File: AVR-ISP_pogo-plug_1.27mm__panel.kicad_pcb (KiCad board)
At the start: 2 copper layers, 96 x 82 mm, 112 parts, among them P1 CONN_6, P2 CONN_6

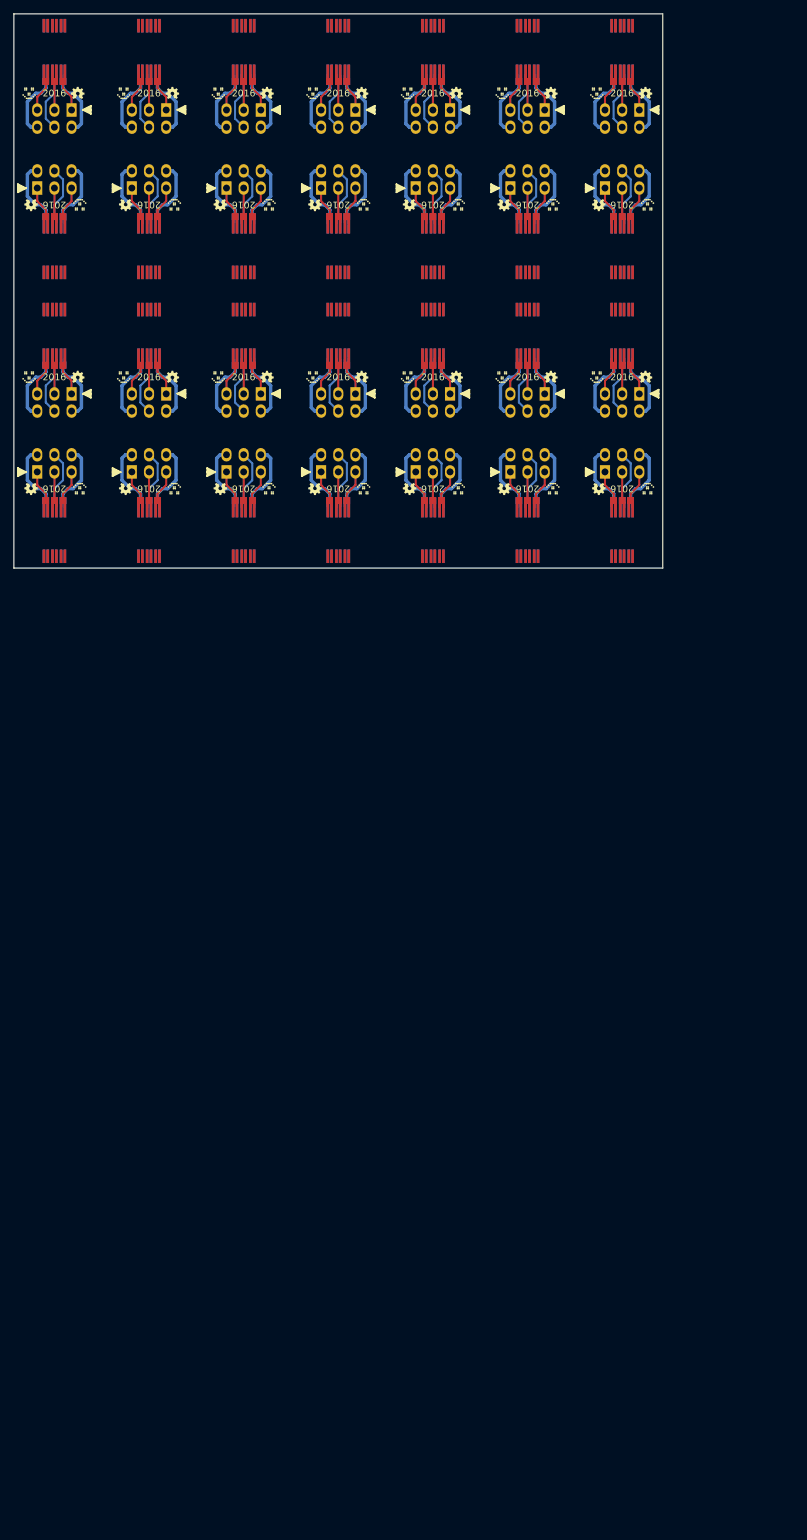
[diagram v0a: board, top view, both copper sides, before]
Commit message: Panel with mouse-bites instead of v-scoring.
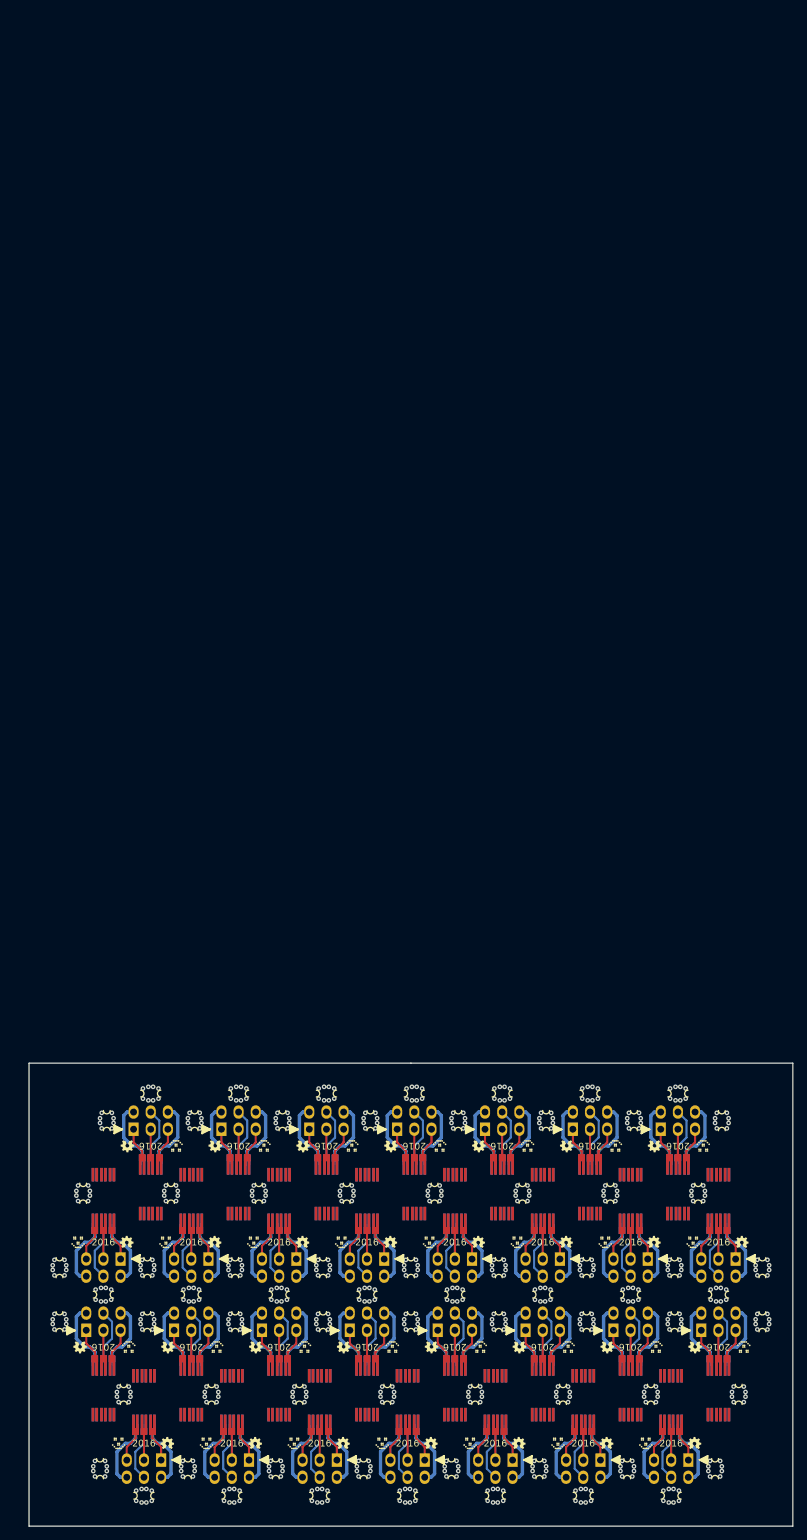
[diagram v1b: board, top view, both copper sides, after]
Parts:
- removed the G1 at (61.2, -97.8)
- removed the G1 at (67.8, -72.2)
- removed the G1 at (81.8, -72.2)
- removed the G1 at (89.2, -97.8)
- removed the G1 at (109.8, -72.2)
- removed the G1 at (117.2, -55.8)
- removed the G1 at (103.2, -55.8)
- removed the G1 at (95.8, -72.2)
- removed the G1 at (109.8, -114.2)
- removed the G1 at (95.8, -114.2)
- removed the G1 at (117.2, -97.8)
- removed the G1 at (61.2, -55.8)
- removed the G1 at (103.2, -97.8)
- removed the G1 at (47.2, -55.8)
- removed the G1 at (39.8, -72.2)
- removed the G1 at (47.2, -97.8)
- removed the G1 at (39.8, -114.2)
- removed the G1 at (25.8, -72.2)
- removed the G1 at (33.2, -55.8)
- removed the G1 at (33.2, -97.8)
- removed the G1 at (25.8, -114.2)
- removed the G1 at (53.8, -114.2)
- removed the G1 at (53.8, -72.2)
- removed the G1 at (89.2, -55.8)
- removed the G1 at (75.2, -55.8)
- removed the G1 at (67.8, -114.2)
- removed the G1 at (75.2, -97.8)
- removed the G1 at (81.8, -114.2)
- removed the G2 at (54.0, -97.7)
- removed the G2 at (75.0, -72.3)
- removed the G2 at (89.0, -72.3)
- removed the G2 at (82.0, -97.7)
- removed the G2 at (117.0, -72.3)
- removed the G2 at (103.0, -72.3)
- removed the G2 at (96.0, -55.7)
- removed the G2 at (110.0, -55.7)
- removed the G2 at (117.0, -114.3)
- removed the G2 at (103.0, -114.3)
- removed the G2 at (110.0, -97.7)
- removed the G2 at (54.0, -55.7)
- removed the G2 at (96.0, -97.7)
- removed the G2 at (40.0, -55.7)
- removed the G2 at (47.0, -72.3)
- removed the G2 at (40.0, -97.7)
- removed the G2 at (47.0, -114.3)
- removed the G2 at (33.0, -72.3)
- removed the G2 at (26.0, -55.7)
- removed the G2 at (33.0, -114.3)
- removed the G2 at (26.0, -97.7)
- removed the G2 at (61.0, -114.3)
- removed the G2 at (61.0, -72.3)
- removed the G2 at (82.0, -55.7)
- removed the G2 at (68.0, -55.7)
- removed the G2 at (68.0, -97.7)
- removed the G2 at (89.0, -114.3)
- removed the G2 at (75.0, -114.3)
- removed the P1 at (57.5, -101.5)
- removed the P1 at (85.5, -68.5)
- removed the P1 at (71.5, -68.5)
- removed the P1 at (85.5, -101.5)
- removed the P1 at (113.5, -68.5)
- removed the P1 at (99.5, -68.5)
- removed the P1 at (113.5, -59.5)
- removed the P1 at (99.5, -59.5)
- removed the P1 at (113.5, -110.5)
- removed the P1 at (99.5, -110.5)
- removed the P1 at (113.5, -101.5)
- removed the P1 at (57.5, -59.5)
- removed the P1 at (99.5, -101.5)
- removed the P1 at (43.5, -59.5)
- removed the P1 at (43.5, -68.5)
- removed the P1 at (43.5, -101.5)
- removed the P1 at (43.5, -110.5)
- removed the P1 at (29.5, -68.5)
- removed the P1 at (29.5, -59.5)
- removed the P1 at (29.5, -110.5)
- removed the P1 at (29.5, -101.5)
- removed the P1 at (57.5, -110.5)
- removed the P1 at (57.5, -68.5)
- removed the P1 at (85.5, -59.5)
- removed the P1 at (71.5, -59.5)
- removed the P1 at (71.5, -101.5)
- removed the P1 at (71.5, -110.5)
- removed the P1 at (85.5, -110.5)
- removed the P2 at (57.5, -91.5)
- removed the P2 at (85.5, -78.5)
- removed the P2 at (85.5, -91.5)
- removed the P2 at (71.5, -91.5)
- removed the P2 at (113.5, -78.5)
- removed the P2 at (113.5, -49.5)
- removed the P2 at (99.5, -49.5)
- removed the P2 at (99.5, -78.5)
- removed the P2 at (113.5, -120.5)
- removed the P2 at (99.5, -120.5)
- removed the P2 at (113.5, -91.5)
- removed the P2 at (57.5, -49.5)
- removed the P2 at (99.5, -91.5)
- removed the P2 at (43.5, -49.5)
- removed the P2 at (43.5, -91.5)
- removed the P2 at (43.5, -78.5)
- removed the P2 at (43.5, -120.5)
- removed the P2 at (29.5, -78.5)
- removed the P2 at (29.5, -49.5)
- removed the P2 at (29.5, -120.5)
- removed the P2 at (29.5, -91.5)
- removed the P2 at (57.5, -120.5)
- removed the P2 at (57.5, -78.5)
- removed the P2 at (85.5, -49.5)
- removed the P2 at (71.5, -49.5)
- removed the P2 at (85.5, -120.5)
- removed the P2 at (71.5, -120.5)
- removed the P2 at (71.5, -78.5)
- added G1: LED_smile_silkscreen_2mm, LED_smile_silkscreen_2mm, F.Cu at (40.5, 71.2)
- added G1: LED_smile_silkscreen_2mm, LED_smile_silkscreen_2mm, F.Cu at (66.5, 71.2)
- added G1: LED_smile_silkscreen_2mm, LED_smile_silkscreen_2mm, F.Cu at (53.5, 71.3)
- added G1: LED_smile_silkscreen_2mm, LED_smile_silkscreen_2mm, F.Cu at (52.0, 85.5)
- added G1: LED_smile_silkscreen_2mm, LED_smile_silkscreen_2mm, F.Cu at (117.0, 85.5)
- added G1: LED_smile_silkscreen_2mm, LED_smile_silkscreen_2mm, F.Cu at (131.5, 71.2)
- added G1: LED_smile_silkscreen_2mm, LED_smile_silkscreen_2mm, F.Cu at (91.0, 85.5)
- added G1: LED_smile_silkscreen_2mm, LED_smile_silkscreen_2mm, F.Cu at (118.5, 71.3)
- added G1: LED_smile_silkscreen_2mm, LED_smile_silkscreen_2mm, F.Cu at (73.5, 41.5)
- added G1: LED_smile_silkscreen_2mm, LED_smile_silkscreen_2mm, F.Cu at (60.5, 41.5)
- added G1: LED_smile_silkscreen_2mm, LED_smile_silkscreen_2mm, F.Cu at (125.5, 41.5)
- added G1: LED_smile_silkscreen_2mm, LED_smile_silkscreen_2mm, F.Cu at (124.0, 55.8)
- added G1: LED_smile_silkscreen_2mm, LED_smile_silkscreen_2mm, F.Cu at (86.5, 41.5)
- added G1: LED_smile_silkscreen_2mm, LED_smile_silkscreen_2mm, F.Cu at (47.5, 41.5)
- added G1: LED_smile_silkscreen_2mm, LED_smile_silkscreen_2mm, F.Cu at (99.5, 41.5)
- added G1: LED_smile_silkscreen_2mm, LED_smile_silkscreen_2mm, F.Cu at (112.5, 41.5)
- added G1: LED_smile_silkscreen_2mm, LED_smile_silkscreen_2mm, F.Cu at (111.0, 55.8)
- added G1: LED_smile_silkscreen_2mm, LED_smile_silkscreen_2mm, F.Cu at (98.0, 55.8)
- added G1: LED_smile_silkscreen_2mm, LED_smile_silkscreen_2mm, F.Cu at (85.0, 55.8)
- added G1: LED_smile_silkscreen_2mm, LED_smile_silkscreen_2mm, F.Cu at (59.0, 55.8)
- added G1: LED_smile_silkscreen_2mm, LED_smile_silkscreen_2mm, F.Cu at (72.0, 55.8)
- added G1: LED_smile_silkscreen_2mm, LED_smile_silkscreen_2mm, F.Cu at (46.0, 55.8)
- added G1: LED_smile_silkscreen_2mm, LED_smile_silkscreen_2mm, F.Cu at (79.5, 71.2)
- added G1: LED_smile_silkscreen_2mm, LED_smile_silkscreen_2mm, F.Cu at (33.0, 55.8)
- added G1: LED_smile_silkscreen_2mm, LED_smile_silkscreen_2mm, F.Cu at (78.0, 85.5)
- added G1: LED_smile_silkscreen_2mm, LED_smile_silkscreen_2mm, F.Cu at (105.5, 71.3)
- added G1: LED_smile_silkscreen_2mm, LED_smile_silkscreen_2mm, F.Cu at (104.0, 85.5)
- added G1: LED_smile_silkscreen_2mm, LED_smile_silkscreen_2mm, F.Cu at (92.5, 71.2)
- added G1: LED_smile_silkscreen_2mm, LED_smile_silkscreen_2mm, F.Cu at (39.0, 85.5)
- added G1: LED_smile_silkscreen_2mm, LED_smile_silkscreen_2mm, F.Cu at (65.0, 85.5)
- added G2: OSHW-logo_silkscreen_2mm, OSHW-logo_silkscreen_2mm, F.Cu at (33.3, 71.3)
- added G2: OSHW-logo_silkscreen_2mm, OSHW-logo_silkscreen_2mm, F.Cu at (59.3, 71.3)
- added G2: OSHW-logo_silkscreen_2mm, OSHW-logo_silkscreen_2mm, F.Cu at (46.3, 71.3)
- added G2: OSHW-logo_silkscreen_2mm, OSHW-logo_silkscreen_2mm, F.Cu at (59.2, 85.5)
- added G2: OSHW-logo_silkscreen_2mm, OSHW-logo_silkscreen_2mm, F.Cu at (111.2, 85.5)
- added G2: OSHW-logo_silkscreen_2mm, OSHW-logo_silkscreen_2mm, F.Cu at (124.2, 85.5)
- added G2: OSHW-logo_silkscreen_2mm, OSHW-logo_silkscreen_2mm, F.Cu at (124.3, 71.3)
- added G2: OSHW-logo_silkscreen_2mm, OSHW-logo_silkscreen_2mm, F.Cu at (111.3, 71.3)
- added G2: OSHW-logo_silkscreen_2mm, OSHW-logo_silkscreen_2mm, F.Cu at (66.3, 41.6)
- added G2: OSHW-logo_silkscreen_2mm, OSHW-logo_silkscreen_2mm, F.Cu at (53.3, 41.5)
- added G2: OSHW-logo_silkscreen_2mm, OSHW-logo_silkscreen_2mm, F.Cu at (118.3, 41.6)
- added G2: OSHW-logo_silkscreen_2mm, OSHW-logo_silkscreen_2mm, F.Cu at (131.2, 55.7)
- added G2: OSHW-logo_silkscreen_2mm, OSHW-logo_silkscreen_2mm, F.Cu at (79.3, 41.5)
- added G2: OSHW-logo_silkscreen_2mm, OSHW-logo_silkscreen_2mm, F.Cu at (40.3, 41.5)
- added G2: OSHW-logo_silkscreen_2mm, OSHW-logo_silkscreen_2mm, F.Cu at (92.3, 41.6)
- added G2: OSHW-logo_silkscreen_2mm, OSHW-logo_silkscreen_2mm, F.Cu at (105.3, 41.5)
- added G2: OSHW-logo_silkscreen_2mm, OSHW-logo_silkscreen_2mm, F.Cu at (118.2, 55.7)
- added G2: OSHW-logo_silkscreen_2mm, OSHW-logo_silkscreen_2mm, F.Cu at (92.2, 55.7)
- added G2: OSHW-logo_silkscreen_2mm, OSHW-logo_silkscreen_2mm, F.Cu at (105.2, 55.7)
- added G2: OSHW-logo_silkscreen_2mm, OSHW-logo_silkscreen_2mm, F.Cu at (66.2, 55.7)
- added G2: OSHW-logo_silkscreen_2mm, OSHW-logo_silkscreen_2mm, F.Cu at (79.2, 55.7)
- added G2: OSHW-logo_silkscreen_2mm, OSHW-logo_silkscreen_2mm, F.Cu at (53.2, 55.7)
- added G2: OSHW-logo_silkscreen_2mm, OSHW-logo_silkscreen_2mm, F.Cu at (72.3, 71.3)
- added G2: OSHW-logo_silkscreen_2mm, OSHW-logo_silkscreen_2mm, F.Cu at (40.2, 55.7)
- added G2: OSHW-logo_silkscreen_2mm, OSHW-logo_silkscreen_2mm, F.Cu at (85.3, 71.3)
- added G2: OSHW-logo_silkscreen_2mm, OSHW-logo_silkscreen_2mm, F.Cu at (85.2, 85.5)
- added G2: OSHW-logo_silkscreen_2mm, OSHW-logo_silkscreen_2mm, F.Cu at (98.3, 71.3)
- added G2: OSHW-logo_silkscreen_2mm, OSHW-logo_silkscreen_2mm, F.Cu at (98.2, 85.5)
- added G2: OSHW-logo_silkscreen_2mm, OSHW-logo_silkscreen_2mm, F.Cu at (72.2, 85.5)
- added G2: OSHW-logo_silkscreen_2mm, OSHW-logo_silkscreen_2mm, F.Cu at (46.2, 85.5)
- added P1: CONN_6, my_parts:MADW__PIN_ARRAY_3x2_2.54mm, F.Cu at (36.8, 67.5)
- added P1: CONN_6, my_parts:MADW__PIN_ARRAY_3x2_2.54mm, F.Cu at (49.7, 67.5)
- added P1: CONN_6, my_parts:MADW__PIN_ARRAY_3x2_2.54mm, F.Cu at (107.8, 89.2)
- added P1: CONN_6, my_parts:MADW__PIN_ARRAY_3x2_2.54mm, F.Cu at (120.8, 89.2)
- added P1: CONN_6, my_parts:MADW__PIN_ARRAY_3x2_2.54mm, F.Cu at (127.8, 67.5)
- added P1: CONN_6, my_parts:MADW__PIN_ARRAY_3x2_2.54mm, F.Cu at (94.8, 89.2)
- added P1: CONN_6, my_parts:MADW__PIN_ARRAY_3x2_2.54mm, F.Cu at (81.8, 89.2)
- added P1: CONN_6, my_parts:MADW__PIN_ARRAY_3x2_2.54mm, F.Cu at (114.8, 67.5)
- added P1: CONN_6, my_parts:MADW__PIN_ARRAY_3x2_2.54mm, F.Cu at (69.7, 37.8)
- added P1: CONN_6, my_parts:MADW__PIN_ARRAY_3x2_2.54mm, F.Cu at (56.8, 37.8)
- added P1: CONN_6, my_parts:MADW__PIN_ARRAY_3x2_2.54mm, F.Cu at (121.8, 37.8)
- added P1: CONN_6, my_parts:MADW__PIN_ARRAY_3x2_2.54mm, F.Cu at (127.8, 59.5)
- added P1: CONN_6, my_parts:MADW__PIN_ARRAY_3x2_2.54mm, F.Cu at (82.7, 37.8)
- added P1: CONN_6, my_parts:MADW__PIN_ARRAY_3x2_2.54mm, F.Cu at (43.7, 37.7)
- added P1: CONN_6, my_parts:MADW__PIN_ARRAY_3x2_2.54mm, F.Cu at (95.8, 37.7)
- added P1: CONN_6, my_parts:MADW__PIN_ARRAY_3x2_2.54mm, F.Cu at (108.8, 37.8)
- added P1: CONN_6, my_parts:MADW__PIN_ARRAY_3x2_2.54mm, F.Cu at (114.8, 59.5)
- added P1: CONN_6, my_parts:MADW__PIN_ARRAY_3x2_2.54mm, F.Cu at (88.8, 59.5)
- added P1: CONN_6, my_parts:MADW__PIN_ARRAY_3x2_2.54mm, F.Cu at (101.8, 59.5)
- added P1: CONN_6, my_parts:MADW__PIN_ARRAY_3x2_2.54mm, F.Cu at (62.8, 59.5)
- added P1: CONN_6, my_parts:MADW__PIN_ARRAY_3x2_2.54mm, F.Cu at (75.8, 59.5)
- added P1: CONN_6, my_parts:MADW__PIN_ARRAY_3x2_2.54mm, F.Cu at (49.8, 59.5)
- added P1: CONN_6, my_parts:MADW__PIN_ARRAY_3x2_2.54mm, F.Cu at (75.7, 67.5)
- added P1: CONN_6, my_parts:MADW__PIN_ARRAY_3x2_2.54mm, F.Cu at (36.8, 59.5)
- added P1: CONN_6, my_parts:MADW__PIN_ARRAY_3x2_2.54mm, F.Cu at (101.8, 67.5)
- added P1: CONN_6, my_parts:MADW__PIN_ARRAY_3x2_2.54mm, F.Cu at (88.7, 67.5)
- added P1: CONN_6, my_parts:MADW__PIN_ARRAY_3x2_2.54mm, F.Cu at (68.8, 89.2)
- added P1: CONN_6, my_parts:MADW__PIN_ARRAY_3x2_2.54mm, F.Cu at (55.8, 89.2)
- added P1: CONN_6, my_parts:MADW__PIN_ARRAY_3x2_2.54mm, F.Cu at (42.8, 89.2)
- added P1: CONN_6, my_parts:MADW__PIN_ARRAY_3x2_2.54mm, F.Cu at (62.8, 67.5)
- added P2: CONN_6, MADW__PIN_ARRAY_3x2_1.27mm, F.Cu at (36.8, 77.5)
- added P2: CONN_6, MADW__PIN_ARRAY_3x2_1.27mm, F.Cu at (68.8, 79.2)
- added P2: CONN_6, MADW__PIN_ARRAY_3x2_1.27mm, F.Cu at (49.8, 77.5)
- added P2: CONN_6, MADW__PIN_ARRAY_3x2_1.27mm, F.Cu at (55.8, 79.2)
- added P2: CONN_6, MADW__PIN_ARRAY_3x2_1.27mm, F.Cu at (42.8, 79.2)
- added P2: CONN_6, MADW__PIN_ARRAY_3x2_1.27mm, F.Cu at (120.8, 79.2)
- added P2: CONN_6, MADW__PIN_ARRAY_3x2_1.27mm, F.Cu at (114.7, 77.5)
- added P2: CONN_6, MADW__PIN_ARRAY_3x2_1.27mm, F.Cu at (127.8, 77.5)
- added P2: CONN_6, MADW__PIN_ARRAY_3x2_1.27mm, F.Cu at (69.8, 47.8)
- added P2: CONN_6, MADW__PIN_ARRAY_3x2_1.27mm, F.Cu at (82.8, 47.8)
- added P2: CONN_6, MADW__PIN_ARRAY_3x2_1.27mm, F.Cu at (121.8, 47.8)
- added P2: CONN_6, MADW__PIN_ARRAY_3x2_1.27mm, F.Cu at (127.8, 49.5)
- added P2: CONN_6, MADW__PIN_ARRAY_3x2_1.27mm, F.Cu at (56.8, 47.8)
- added P2: CONN_6, MADW__PIN_ARRAY_3x2_1.27mm, F.Cu at (43.8, 47.7)
- added P2: CONN_6, MADW__PIN_ARRAY_3x2_1.27mm, F.Cu at (95.8, 47.8)
- added P2: CONN_6, MADW__PIN_ARRAY_3x2_1.27mm, F.Cu at (108.7, 47.7)
- added P2: CONN_6, MADW__PIN_ARRAY_3x2_1.27mm, F.Cu at (114.8, 49.5)
- added P2: CONN_6, MADW__PIN_ARRAY_3x2_1.27mm, F.Cu at (101.8, 49.5)
- added P2: CONN_6, MADW__PIN_ARRAY_3x2_1.27mm, F.Cu at (88.8, 49.5)
- added P2: CONN_6, MADW__PIN_ARRAY_3x2_1.27mm, F.Cu at (62.8, 49.5)
- added P2: CONN_6, MADW__PIN_ARRAY_3x2_1.27mm, F.Cu at (75.8, 49.5)
- added P2: CONN_6, MADW__PIN_ARRAY_3x2_1.27mm, F.Cu at (49.8, 49.5)
- added P2: CONN_6, MADW__PIN_ARRAY_3x2_1.27mm, F.Cu at (81.8, 79.2)
- added P2: CONN_6, MADW__PIN_ARRAY_3x2_1.27mm, F.Cu at (36.8, 49.5)
- added P2: CONN_6, MADW__PIN_ARRAY_3x2_1.27mm, F.Cu at (75.8, 77.5)
- added P2: CONN_6, MADW__PIN_ARRAY_3x2_1.27mm, F.Cu at (107.8, 79.2)
- added P2: CONN_6, MADW__PIN_ARRAY_3x2_1.27mm, F.Cu at (101.8, 77.5)
- added P2: CONN_6, MADW__PIN_ARRAY_3x2_1.27mm, F.Cu at (94.8, 79.2)
- added P2: CONN_6, MADW__PIN_ARRAY_3x2_1.27mm, F.Cu at (88.8, 77.5)
- added P2: CONN_6, MADW__PIN_ARRAY_3x2_1.27mm, F.Cu at (62.8, 77.5)
- added mouse-bite-1mm-slot: VAL**, Panelization:mouse-bite-1mm-slot, F.Cu at (33.8, 48.5)
- added mouse-bite-1mm-slot: VAL**, Panelization:mouse-bite-1mm-slot, F.Cu at (91.8, 78.2)
- added mouse-bite-1mm-slot: VAL**, Panelization:mouse-bite-1mm-slot, F.Cu at (95.2, 67.5)
- added mouse-bite-1mm-slot: VAL**, Panelization:mouse-bite-1mm-slot, F.Cu at (75.2, 89.2)
- added mouse-bite-1mm-slot: VAL**, Panelization:mouse-bite-1mm-slot, F.Cu at (62.2, 89.2)
- added mouse-bite-1mm-slot: VAL**, Panelization:mouse-bite-1mm-slot, F.Cu at (49.2, 89.2)
- added mouse-bite-1mm-slot: VAL**, Panelization:mouse-bite-1mm-slot, F.Cu at (69.2, 67.5)
- added mouse-bite-1mm-slot: VAL**, Panelization:mouse-bite-1mm-slot, F.Cu at (56.2, 67.5)
- added mouse-bite-1mm-slot: VAL**, Panelization:mouse-bite-1mm-slot, F.Cu at (65.8, 78.2)
- added mouse-bite-1mm-slot: VAL**, Panelization:mouse-bite-1mm-slot, F.Cu at (52.8, 78.2)
- added mouse-bite-1mm-slot: VAL**, Panelization:mouse-bite-1mm-slot, F.Cu at (101.2, 89.2)
- added mouse-bite-1mm-slot: VAL**, Panelization:mouse-bite-1mm-slot, F.Cu at (128.2, 37.8)
- added mouse-bite-1mm-slot: VAL**, Panelization:mouse-bite-1mm-slot, F.Cu at (114.2, 89.2)
- added mouse-bite-1mm-slot: VAL**, Panelization:mouse-bite-1mm-slot, F.Cu at (117.8, 78.2)
- added mouse-bite-1mm-slot: VAL**, Panelization:mouse-bite-1mm-slot, F.Cu at (88.2, 89.2)
- added mouse-bite-1mm-slot: VAL**, Panelization:mouse-bite-1mm-slot, F.Cu at (121.2, 67.5)
- added mouse-bite-1mm-slot: VAL**, Panelization:mouse-bite-1mm-slot, F.Cu at (111.8, 48.5)
- added mouse-bite-1mm-slot: VAL**, Panelization:mouse-bite-1mm-slot, F.Cu at (98.8, 48.5)
- added mouse-bite-1mm-slot: VAL**, Panelization:mouse-bite-1mm-slot, F.Cu at (85.8, 48.5)
- added mouse-bite-1mm-slot: VAL**, Panelization:mouse-bite-1mm-slot, F.Cu at (72.8, 48.5)
- added mouse-bite-1mm-slot: VAL**, Panelization:mouse-bite-1mm-slot, F.Cu at (59.8, 48.5)
- added mouse-bite-1mm-slot: VAL**, Panelization:mouse-bite-1mm-slot, F.Cu at (76.2, 37.8)
- added mouse-bite-1mm-slot: VAL**, Panelization:mouse-bite-1mm-slot, F.Cu at (124.8, 48.5)
- added mouse-bite-1mm-slot: VAL**, Panelization:mouse-bite-1mm-slot, F.Cu at (63.2, 37.7)
- added mouse-bite-1mm-slot: VAL**, Panelization:mouse-bite-1mm-slot, F.Cu at (89.2, 37.8)
- added mouse-bite-1mm-slot: VAL**, Panelization:mouse-bite-1mm-slot, F.Cu at (50.2, 37.8)
- added mouse-bite-1mm-slot: VAL**, Panelization:mouse-bite-1mm-slot, F.Cu at (102.2, 37.7)
- added mouse-bite-1mm-slot: VAL**, Panelization:mouse-bite-1mm-slot, F.Cu at (115.2, 37.8)
- added mouse-bite-1mm-slot: VAL**, Panelization:mouse-bite-1mm-slot, F.Cu at (82.2, 59.5)
- added mouse-bite-1mm-slot: VAL**, Panelization:mouse-bite-1mm-slot, F.Cu at (108.2, 59.5)
- added mouse-bite-1mm-slot: VAL**, Panelization:mouse-bite-1mm-slot, F.Cu at (95.2, 59.5)
- added mouse-bite-1mm-slot: VAL**, Panelization:mouse-bite-1mm-slot, F.Cu at (56.2, 59.5)
- added mouse-bite-1mm-slot: VAL**, Panelization:mouse-bite-1mm-slot, F.Cu at (69.2, 59.5)
- added mouse-bite-1mm-slot: VAL**, Panelization:mouse-bite-1mm-slot, F.Cu at (130.8, 78.2)
- added mouse-bite-1mm-slot: VAL**, Panelization:mouse-bite-1mm-slot, F.Cu at (43.2, 59.5)
- added mouse-bite-1mm-slot: VAL**, Panelization:mouse-bite-1mm-slot, F.Cu at (46.8, 48.5)
- added mouse-bite-1mm-slot: VAL**, Panelization:mouse-bite-1mm-slot, F.Cu at (49.8, 63.5)
- added mouse-bite-1mm-slot: VAL**, Panelization:mouse-bite-1mm-slot, F.Cu at (62.8, 63.5)
- added mouse-bite-1mm-slot: VAL**, Panelization:mouse-bite-1mm-slot, F.Cu at (75.8, 63.5)
- added mouse-bite-1mm-slot: VAL**, Panelization:mouse-bite-1mm-slot, F.Cu at (88.8, 63.5)
- added mouse-bite-1mm-slot: VAL**, Panelization:mouse-bite-1mm-slot, F.Cu at (101.8, 63.5)
- added mouse-bite-1mm-slot: VAL**, Panelization:mouse-bite-1mm-slot, F.Cu at (114.8, 63.5)
- added mouse-bite-1mm-slot: VAL**, Panelization:mouse-bite-1mm-slot, F.Cu at (36.8, 63.5)
- added mouse-bite-1mm-slot: VAL**, Panelization:mouse-bite-1mm-slot, F.Cu at (127.8, 63.5)
- added mouse-bite-1mm-slot: VAL**, Panelization:mouse-bite-1mm-slot, F.Cu at (39.8, 78.2)
- added mouse-bite-1mm-slot: VAL**, Panelization:mouse-bite-1mm-slot, F.Cu at (121.8, 33.8)
- added mouse-bite-1mm-slot: VAL**, Panelization:mouse-bite-1mm-slot, F.Cu at (108.8, 33.8)
- added mouse-bite-1mm-slot: VAL**, Panelization:mouse-bite-1mm-slot, F.Cu at (95.8, 33.8)
- added mouse-bite-1mm-slot: VAL**, Panelization:mouse-bite-1mm-slot, F.Cu at (82.8, 33.8)
- added mouse-bite-1mm-slot: VAL**, Panelization:mouse-bite-1mm-slot, F.Cu at (69.8, 33.8)
- added mouse-bite-1mm-slot: VAL**, Panelization:mouse-bite-1mm-slot, F.Cu at (56.8, 33.8)
- added mouse-bite-1mm-slot: VAL**, Panelization:mouse-bite-1mm-slot, F.Cu at (43.8, 33.8)
- added mouse-bite-1mm-slot: VAL**, Panelization:mouse-bite-1mm-slot, F.Cu at (42.8, 93.2)
- added mouse-bite-1mm-slot: VAL**, Panelization:mouse-bite-1mm-slot, F.Cu at (55.8, 93.2)
- added mouse-bite-1mm-slot: VAL**, Panelization:mouse-bite-1mm-slot, F.Cu at (68.8, 93.2)
- added mouse-bite-1mm-slot: VAL**, Panelization:mouse-bite-1mm-slot, F.Cu at (82.2, 67.5)
- added mouse-bite-1mm-slot: VAL**, Panelization:mouse-bite-1mm-slot, F.Cu at (81.8, 93.2)
- added mouse-bite-1mm-slot: VAL**, Panelization:mouse-bite-1mm-slot, F.Cu at (94.8, 93.2)
- added mouse-bite-1mm-slot: VAL**, Panelization:mouse-bite-1mm-slot, F.Cu at (107.8, 93.2)
- added mouse-bite-1mm-slot: VAL**, Panelization:mouse-bite-1mm-slot, F.Cu at (120.8, 93.2)
- added mouse-bite-1mm-slot: VAL**, Panelization:mouse-bite-1mm-slot, F.Cu at (30.2, 59.5)
- added mouse-bite-1mm-slot: VAL**, Panelization:mouse-bite-1mm-slot, F.Cu at (30.2, 67.5)
- added mouse-bite-1mm-slot: VAL**, Panelization:mouse-bite-1mm-slot, F.Cu at (134.2, 67.5)
- added mouse-bite-1mm-slot: VAL**, Panelization:mouse-bite-1mm-slot, F.Cu at (134.2, 59.5)
- added mouse-bite-1mm-slot: VAL**, Panelization:mouse-bite-1mm-slot, F.Cu at (36.2, 89.2)
- added mouse-bite-1mm-slot: VAL**, Panelization:mouse-bite-1mm-slot, F.Cu at (127.2, 89.2)
- added mouse-bite-1mm-slot: VAL**, Panelization:mouse-bite-1mm-slot, F.Cu at (78.8, 78.2)
- added mouse-bite-1mm-slot: VAL**, Panelization:mouse-bite-1mm-slot, F.Cu at (121.2, 59.5)
- added mouse-bite-1mm-slot: VAL**, Panelization:mouse-bite-1mm-slot, F.Cu at (43.2, 67.5)
- added mouse-bite-1mm-slot: VAL**, Panelization:mouse-bite-1mm-slot, F.Cu at (37.2, 37.8)
- added mouse-bite-1mm-slot: VAL**, Panelization:mouse-bite-1mm-slot, F.Cu at (108.2, 67.5)
- added mouse-bite-1mm-slot: VAL**, Panelization:mouse-bite-1mm-slot, F.Cu at (104.8, 78.2)
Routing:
- net /V-target: track 328.7 -> 352.2 mm
- net /GND: track 328.7 -> 352.2 mm
- net /MOSI: track 281.9 -> 302.1 mm
- net /RESET: track 196.0 -> 210.0 mm
- net /MISO: track 196.0 -> 210.0 mm
- net /SCK: track 180.8 -> 193.7 mm
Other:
- board size 96 x 82 mm -> 113 x 68.5 mm
- board text removed: "ROUTE"
- board text removed: "V-score"

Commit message: Well... routing paths should really be correct.
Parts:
- removed the G1 at (40.5, 71.2)
- removed the G1 at (66.5, 71.2)
- removed the G1 at (53.5, 71.3)
- removed the G1 at (52.0, 85.5)
- removed the G1 at (117.0, 85.5)
- removed the G1 at (131.5, 71.2)
- removed the G1 at (91.0, 85.5)
- removed the G1 at (118.5, 71.3)
- removed the G1 at (79.5, 71.2)
- removed the G1 at (78.0, 85.5)
- removed the G1 at (105.5, 71.3)
- removed the G1 at (104.0, 85.5)
- removed the G1 at (92.5, 71.2)
- removed the G1 at (39.0, 85.5)
- removed the G1 at (65.0, 85.5)
- removed the G2 at (59.3, 71.3)
- removed the G2 at (46.3, 71.3)
- removed the G2 at (59.2, 85.5)
- removed the G2 at (111.2, 85.5)
- removed the G2 at (124.2, 85.5)
- removed the G2 at (124.3, 71.3)
- removed the G2 at (111.3, 71.3)
- removed the G2 at (72.3, 71.3)
- removed the G2 at (85.3, 71.3)
- removed the G2 at (85.2, 85.5)
- removed the G2 at (98.3, 71.3)
- removed the G2 at (98.2, 85.5)
- removed the G2 at (72.2, 85.5)
- removed the G2 at (46.2, 85.5)
- removed the P1 at (36.8, 67.5)
- removed the P1 at (49.7, 67.5)
- removed the P1 at (107.8, 89.2)
- removed the P1 at (120.8, 89.2)
- removed the P1 at (127.8, 67.5)
- removed the P1 at (94.8, 89.2)
- removed the P1 at (81.8, 89.2)
- removed the P1 at (114.8, 67.5)
- removed the P1 at (75.7, 67.5)
- removed the P1 at (101.8, 67.5)
- removed the P1 at (88.7, 67.5)
- removed the P1 at (68.8, 89.2)
- removed the P1 at (55.8, 89.2)
- removed the P1 at (42.8, 89.2)
- removed the P1 at (62.8, 67.5)
- removed the P2 at (36.8, 77.5)
- removed the P2 at (49.8, 77.5)
- removed the P2 at (55.8, 79.2)
- removed the P2 at (42.8, 79.2)
- removed the P2 at (120.8, 79.2)
- removed the P2 at (114.7, 77.5)
- removed the P2 at (127.8, 77.5)
- removed the P2 at (81.8, 79.2)
- removed the P2 at (75.8, 77.5)
- removed the P2 at (107.8, 79.2)
- removed the P2 at (101.8, 77.5)
- removed the P2 at (94.8, 79.2)
- removed the P2 at (88.8, 77.5)
- removed the P2 at (62.8, 77.5)
- removed the mouse-bite-1mm-slot at (91.8, 78.2)
- removed the mouse-bite-1mm-slot at (95.2, 67.5)
- removed the mouse-bite-1mm-slot at (75.2, 89.2)
- removed the mouse-bite-1mm-slot at (62.2, 89.2)
- removed the mouse-bite-1mm-slot at (49.2, 89.2)
- removed the mouse-bite-1mm-slot at (69.2, 67.5)
- removed the mouse-bite-1mm-slot at (56.2, 67.5)
- removed the mouse-bite-1mm-slot at (65.8, 78.2)
- removed the mouse-bite-1mm-slot at (52.8, 78.2)
- removed the mouse-bite-1mm-slot at (101.2, 89.2)
- removed the mouse-bite-1mm-slot at (114.2, 89.2)
- removed the mouse-bite-1mm-slot at (117.8, 78.2)
- removed the mouse-bite-1mm-slot at (88.2, 89.2)
- removed the mouse-bite-1mm-slot at (121.2, 67.5)
- removed the mouse-bite-1mm-slot at (130.8, 78.2)
- removed the mouse-bite-1mm-slot at (39.8, 78.2)
- removed the mouse-bite-1mm-slot at (42.8, 93.2)
- removed the mouse-bite-1mm-slot at (55.8, 93.2)
- removed the mouse-bite-1mm-slot at (68.8, 93.2)
- removed the mouse-bite-1mm-slot at (82.2, 67.5)
- removed the mouse-bite-1mm-slot at (81.8, 93.2)
- removed the mouse-bite-1mm-slot at (94.8, 93.2)
- removed the mouse-bite-1mm-slot at (107.8, 93.2)
- removed the mouse-bite-1mm-slot at (120.8, 93.2)
- removed the mouse-bite-1mm-slot at (30.2, 67.5)
- removed the mouse-bite-1mm-slot at (134.2, 67.5)
- removed the mouse-bite-1mm-slot at (36.2, 89.2)
- removed the mouse-bite-1mm-slot at (127.2, 89.2)
- removed the mouse-bite-1mm-slot at (78.8, 78.2)
- removed the mouse-bite-1mm-slot at (43.2, 67.5)
- removed the mouse-bite-1mm-slot at (108.2, 67.5)
- removed the mouse-bite-1mm-slot at (104.8, 78.2)
- added G1: LED_smile_silkscreen_2mm, LED_smile_silkscreen_2mm, F.Cu at (118.5, 71.3)
- added G1: LED_smile_silkscreen_2mm, LED_smile_silkscreen_2mm, F.Cu at (40.5, 71.3)
- added G1: LED_smile_silkscreen_2mm, LED_smile_silkscreen_2mm, F.Cu at (66.5, 71.2)
- added G1: LED_smile_silkscreen_2mm, LED_smile_silkscreen_2mm, F.Cu at (79.5, 71.3)
- added G1: LED_smile_silkscreen_2mm, LED_smile_silkscreen_2mm, F.Cu at (92.5, 71.2)
- added G1: LED_smile_silkscreen_2mm, LED_smile_silkscreen_2mm, F.Cu at (78.0, 85.5)
- added G1: LED_smile_silkscreen_2mm, LED_smile_silkscreen_2mm, F.Cu at (91.0, 85.5)
- added G1: LED_smile_silkscreen_2mm, LED_smile_silkscreen_2mm, F.Cu at (105.5, 71.2)
- added G1: LED_smile_silkscreen_2mm, LED_smile_silkscreen_2mm, F.Cu at (131.5, 71.2)
- added G1: LED_smile_silkscreen_2mm, LED_smile_silkscreen_2mm, F.Cu at (117.0, 85.5)
- added G1: LED_smile_silkscreen_2mm, LED_smile_silkscreen_2mm, F.Cu at (104.0, 85.5)
- added G1: LED_smile_silkscreen_2mm, LED_smile_silkscreen_2mm, F.Cu at (53.5, 71.2)
- added G1: LED_smile_silkscreen_2mm, LED_smile_silkscreen_2mm, F.Cu at (39.0, 85.5)
- added G1: LED_smile_silkscreen_2mm, LED_smile_silkscreen_2mm, F.Cu at (65.0, 85.5)
- added G1: LED_smile_silkscreen_2mm, LED_smile_silkscreen_2mm, F.Cu at (52.0, 85.5)
- added G2: OSHW-logo_silkscreen_2mm, OSHW-logo_silkscreen_2mm, F.Cu at (111.3, 71.3)
- added G2: OSHW-logo_silkscreen_2mm, OSHW-logo_silkscreen_2mm, F.Cu at (59.3, 71.3)
- added G2: OSHW-logo_silkscreen_2mm, OSHW-logo_silkscreen_2mm, F.Cu at (72.2, 85.4)
- added G2: OSHW-logo_silkscreen_2mm, OSHW-logo_silkscreen_2mm, F.Cu at (72.3, 71.3)
- added G2: OSHW-logo_silkscreen_2mm, OSHW-logo_silkscreen_2mm, F.Cu at (85.3, 71.3)
- added G2: OSHW-logo_silkscreen_2mm, OSHW-logo_silkscreen_2mm, F.Cu at (85.2, 85.5)
- added G2: OSHW-logo_silkscreen_2mm, OSHW-logo_silkscreen_2mm, F.Cu at (98.2, 85.4)
- added G2: OSHW-logo_silkscreen_2mm, OSHW-logo_silkscreen_2mm, F.Cu at (98.3, 71.3)
- added G2: OSHW-logo_silkscreen_2mm, OSHW-logo_silkscreen_2mm, F.Cu at (124.3, 71.3)
- added G2: OSHW-logo_silkscreen_2mm, OSHW-logo_silkscreen_2mm, F.Cu at (124.2, 85.5)
- added G2: OSHW-logo_silkscreen_2mm, OSHW-logo_silkscreen_2mm, F.Cu at (111.2, 85.4)
- added G2: OSHW-logo_silkscreen_2mm, OSHW-logo_silkscreen_2mm, F.Cu at (46.3, 71.3)
- added G2: OSHW-logo_silkscreen_2mm, OSHW-logo_silkscreen_2mm, F.Cu at (46.2, 85.4)
- added G2: OSHW-logo_silkscreen_2mm, OSHW-logo_silkscreen_2mm, F.Cu at (59.2, 85.5)
- added P1: CONN_6, my_parts:MADW__PIN_ARRAY_3x2_2.54mm, F.Cu at (114.8, 67.5)
- added P1: CONN_6, my_parts:MADW__PIN_ARRAY_3x2_2.54mm, F.Cu at (55.8, 89.2)
- added P1: CONN_6, my_parts:MADW__PIN_ARRAY_3x2_2.54mm, F.Cu at (62.7, 67.5)
- added P1: CONN_6, my_parts:MADW__PIN_ARRAY_3x2_2.54mm, F.Cu at (75.7, 67.5)
- added P1: CONN_6, my_parts:MADW__PIN_ARRAY_3x2_2.54mm, F.Cu at (88.8, 67.5)
- added P1: CONN_6, my_parts:MADW__PIN_ARRAY_3x2_2.54mm, F.Cu at (81.8, 89.2)
- added P1: CONN_6, my_parts:MADW__PIN_ARRAY_3x2_2.54mm, F.Cu at (94.8, 89.2)
- added P1: CONN_6, my_parts:MADW__PIN_ARRAY_3x2_2.54mm, F.Cu at (101.8, 67.5)
- added P1: CONN_6, my_parts:MADW__PIN_ARRAY_3x2_2.54mm, F.Cu at (127.8, 67.5)
- added P1: CONN_6, my_parts:MADW__PIN_ARRAY_3x2_2.54mm, F.Cu at (120.8, 89.3)
- added P1: CONN_6, my_parts:MADW__PIN_ARRAY_3x2_2.54mm, F.Cu at (107.8, 89.2)
- added P1: CONN_6, my_parts:MADW__PIN_ARRAY_3x2_2.54mm, F.Cu at (36.7, 67.5)
- added P1: CONN_6, my_parts:MADW__PIN_ARRAY_3x2_2.54mm, F.Cu at (49.8, 67.5)
- added P1: CONN_6, my_parts:MADW__PIN_ARRAY_3x2_2.54mm, F.Cu at (42.8, 89.2)
- added P1: CONN_6, my_parts:MADW__PIN_ARRAY_3x2_2.54mm, F.Cu at (68.8, 89.3)
- added P2: CONN_6, MADW__PIN_ARRAY_3x2_1.27mm, F.Cu at (114.7, 77.5)
- added P2: CONN_6, MADW__PIN_ARRAY_3x2_1.27mm, F.Cu at (36.7, 77.5)
- added P2: CONN_6, MADW__PIN_ARRAY_3x2_1.27mm, F.Cu at (42.8, 79.2)
- added P2: CONN_6, MADW__PIN_ARRAY_3x2_1.27mm, F.Cu at (81.7, 79.2)
- added P2: CONN_6, MADW__PIN_ARRAY_3x2_1.27mm, F.Cu at (75.8, 77.5)
- added P2: CONN_6, MADW__PIN_ARRAY_3x2_1.27mm, F.Cu at (88.8, 77.5)
- added P2: CONN_6, MADW__PIN_ARRAY_3x2_1.27mm, F.Cu at (94.7, 79.2)
- added P2: CONN_6, MADW__PIN_ARRAY_3x2_1.27mm, F.Cu at (101.8, 77.5)
- added P2: CONN_6, MADW__PIN_ARRAY_3x2_1.27mm, F.Cu at (127.7, 77.5)
- added P2: CONN_6, MADW__PIN_ARRAY_3x2_1.27mm, F.Cu at (120.8, 79.3)
- added P2: CONN_6, MADW__PIN_ARRAY_3x2_1.27mm, F.Cu at (107.8, 79.3)
- added P2: CONN_6, MADW__PIN_ARRAY_3x2_1.27mm, F.Cu at (62.8, 77.5)
- added P2: CONN_6, MADW__PIN_ARRAY_3x2_1.27mm, F.Cu at (55.8, 79.3)
- added P2: CONN_6, MADW__PIN_ARRAY_3x2_1.27mm, F.Cu at (49.8, 77.5)
- added mouse-bite-1mm-slot: VAL**, Panelization:mouse-bite-1mm-slot, F.Cu at (121.2, 68.8)
- added mouse-bite-1mm-slot: VAL**, Panelization:mouse-bite-1mm-slot, F.Cu at (101.2, 88.0)
- added mouse-bite-1mm-slot: VAL**, Panelization:mouse-bite-1mm-slot, F.Cu at (107.7, 93.2)
- added mouse-bite-1mm-slot: VAL**, Panelization:mouse-bite-1mm-slot, F.Cu at (30.2, 68.8)
- added mouse-bite-1mm-slot: VAL**, Panelization:mouse-bite-1mm-slot, F.Cu at (56.2, 68.8)
- added mouse-bite-1mm-slot: VAL**, Panelization:mouse-bite-1mm-slot, F.Cu at (43.2, 68.8)
- added mouse-bite-1mm-slot: VAL**, Panelization:mouse-bite-1mm-slot, F.Cu at (36.2, 88.0)
- added mouse-bite-1mm-slot: VAL**, Panelization:mouse-bite-1mm-slot, F.Cu at (42.8, 93.3)
- added mouse-bite-1mm-slot: VAL**, Panelization:mouse-bite-1mm-slot, F.Cu at (62.3, 88.0)
- added mouse-bite-1mm-slot: VAL**, Panelization:mouse-bite-1mm-slot, F.Cu at (68.8, 93.3)
- added mouse-bite-1mm-slot: VAL**, Panelization:mouse-bite-1mm-slot, F.Cu at (65.8, 78.5)
- added mouse-bite-1mm-slot: VAL**, Panelization:mouse-bite-1mm-slot, F.Cu at (117.7, 78.5)
- added mouse-bite-1mm-slot: VAL**, Panelization:mouse-bite-1mm-slot, F.Cu at (49.2, 88.0)
- added mouse-bite-1mm-slot: VAL**, Panelization:mouse-bite-1mm-slot, F.Cu at (52.7, 78.5)
- added mouse-bite-1mm-slot: VAL**, Panelization:mouse-bite-1mm-slot, F.Cu at (55.8, 93.3)
- added mouse-bite-1mm-slot: VAL**, Panelization:mouse-bite-1mm-slot, F.Cu at (39.8, 78.5)
- added mouse-bite-1mm-slot: VAL**, Panelization:mouse-bite-1mm-slot, F.Cu at (69.2, 68.8)
- added mouse-bite-1mm-slot: VAL**, Panelization:mouse-bite-1mm-slot, F.Cu at (78.8, 78.5)
- added mouse-bite-1mm-slot: VAL**, Panelization:mouse-bite-1mm-slot, F.Cu at (82.2, 68.8)
- added mouse-bite-1mm-slot: VAL**, Panelization:mouse-bite-1mm-slot, F.Cu at (95.2, 68.8)
- added mouse-bite-1mm-slot: VAL**, Panelization:mouse-bite-1mm-slot, F.Cu at (75.2, 88.0)
- added mouse-bite-1mm-slot: VAL**, Panelization:mouse-bite-1mm-slot, F.Cu at (81.8, 93.3)
- added mouse-bite-1mm-slot: VAL**, Panelization:mouse-bite-1mm-slot, F.Cu at (108.2, 68.8)
- added mouse-bite-1mm-slot: VAL**, Panelization:mouse-bite-1mm-slot, F.Cu at (88.2, 88.0)
- added mouse-bite-1mm-slot: VAL**, Panelization:mouse-bite-1mm-slot, F.Cu at (94.7, 93.2)
- added mouse-bite-1mm-slot: VAL**, Panelization:mouse-bite-1mm-slot, F.Cu at (91.8, 78.5)
- added mouse-bite-1mm-slot: VAL**, Panelization:mouse-bite-1mm-slot, F.Cu at (104.7, 78.5)
- added mouse-bite-1mm-slot: VAL**, Panelization:mouse-bite-1mm-slot, F.Cu at (134.3, 68.8)
- added mouse-bite-1mm-slot: VAL**, Panelization:mouse-bite-1mm-slot, F.Cu at (130.8, 78.5)
- added mouse-bite-1mm-slot: VAL**, Panelization:mouse-bite-1mm-slot, F.Cu at (114.2, 88.0)
- added mouse-bite-1mm-slot: VAL**, Panelization:mouse-bite-1mm-slot, F.Cu at (127.2, 88.0)
- added mouse-bite-1mm-slot: VAL**, Panelization:mouse-bite-1mm-slot, F.Cu at (120.8, 93.3)
- moved mouse-bite-1mm-slot 1.25 mm to (102.2, 39.0)
- moved mouse-bite-1mm-slot 1.25 mm to (63.2, 39.0)
- moved mouse-bite-1mm-slot 1.25 mm to (128.2, 39.0)
- moved mouse-bite-1mm-slot 1.25 mm to (76.2, 39.0)
- moved mouse-bite-1mm-slot 1.25 mm to (89.2, 39.0)
- moved mouse-bite-1mm-slot 1.25 mm to (115.2, 39.0)
- moved mouse-bite-1mm-slot 1.25 mm to (82.2, 58.2)
- moved mouse-bite-1mm-slot 1.25 mm to (108.2, 58.2)
- moved mouse-bite-1mm-slot 1.25 mm to (95.2, 58.2)
- moved mouse-bite-1mm-slot 1.25 mm to (56.2, 58.2)
- moved mouse-bite-1mm-slot 1.25 mm to (69.2, 58.2)
- moved mouse-bite-1mm-slot 1.25 mm to (43.2, 58.2)
- moved mouse-bite-1mm-slot 1.25 mm to (30.2, 58.2)
- moved mouse-bite-1mm-slot 1.25 mm to (134.2, 58.2)
- moved mouse-bite-1mm-slot 1.25 mm to (121.2, 58.2)
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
